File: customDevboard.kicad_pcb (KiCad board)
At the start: 2 copper layers, 39 x 39 mm, 79 parts, among them J1 USB_C_Receptacle_USB2.0_14P, J10 GPIO29_ADC3, J11 GND, J12 GPIO0, J13 GPIO1, J14 GPIO2, J15 GPIO3, J16 GPIO4, J17 GPIO5, J18 GPIO6, J19 GPIO7, J2 RUN, J20 GPIO8, J21 GPIO9, J22 Conn_01x01, J23 Conn_01x01, J24 Conn_01x01, J25 Conn_01x01, J26 Conn_01x01, J27 Conn_01x01, J28 Conn_01x01, J29 Conn_01x01, J3 3V3, J30 Conn_01x01, J31 Conn_01x01, J32 Conn_01x01, J33 Conn_01x01, J34 Conn_01x01, J35 Conn_01x01, J36 Conn_01x01, J37 Conn_01x01, J38 Conn_01x01, J39 Conn_01x01, J4 VBUS, J40 Conn_01x01, J41 Conn_01x01, J42 SWCLK, J43 GND, J44 SWD, J5 GND, J6 GND, J7 GPIO26_ADC0, J8 GPIO27_ADC1, J9 GPIO28_ADC2, SW1 BOOT, U1 RP2040, U2 W25Q128JVP, U3 TLV75733PDRV, Y1 12 MHz

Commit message: V1 testing release
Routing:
- net GND: vias 47 -> 48
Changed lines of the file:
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@@
+	)
+	(via
+		(at 66.5 72.5)
+		(size 0.6)
+		(drill 0.3)
+		(layers "F.Cu" "B.Cu")
+		(free yes)
+		(net 1)
 	)
 	(via
@@
 	)
 	(segment
+		(start 71.25 68.343656)
+		(end 71.25 67.75)
+		(width 0.2)
+		(layer "F.Cu")
+		(net 44)
+	)
+	(segment
+		(start 72.25 66.75)
+		(end 72.25 65.5)
+		(width 0.2)
+		(layer "F.Cu")
+		(net 44)
+	)
+	(segment
+		(start 72.5 70.5)
+		(end 71.25 69.25)
+		(width 0.2)
+		(layer "F.Cu")
+		(net 44)
+	)
+	(segment
+		(start 71.65 64.9)
+		(end 69.625 64.9)
+		(width 0.2)
+		(layer "F.Cu")
+		(net 44)
+	)
+	(segment
+		(start 71.25 68.493445)
+		(end 71.25 68.343656)
+		(width 0.2)
+		(layer "F.Cu")
+		(net 44)
+	)
+	(segment
 		(start 71.25 69.25)
+		(end 71.25 68.493445)
+		(width 0.2)
+		(layer "F.Cu")
+		(net 44)
+	)
+	(segment
+		(start 73.75 70.5)
 		(end 72.5 70.5)
 		(width 0.2)
@@
 	)
 	(segment
-		(start 72.25 66.75)
-		(end 71.25 67.75)
+		(start 72.25 65.5)
+		(end 71.65 64.9)
 		(width 0.2)
 		(layer "F.Cu")
@@
 	)
 	(segment
-		(start 72.5 70.5)
-		(end 73.75 70.5)
+		(start 71.25 67.75)
+		(end 72.25 66.75)
 		(width 0.2)
 		(layer "F.Cu")
@@
 	)
 	(segment
-		(start 71.65 64.9)
-		(end 72.25 65.5)
-		(width 0.2)
-		(layer "F.Cu")
-		(net 44)
-	)
-	(segment
-		(start 72.25 65.5)
-		(end 72.25 66.75)
-		(width 0.2)
-		(layer "F.Cu")
-		(net 44)
-	)
-	(segment
-		(start 69.625 64.9)
-		(end 71.65 64.9)
-		(width 0.2)
-		(layer "F.Cu")
-		(net 44)
-	)
-	(segment
-		(start 71.25 67.75)
-		(end 71.25 69.25)
-		(width 0.2)
-		(layer "F.Cu")
-		(net 44)
+		(start 70.75 68.523403)
+		(end 70.75 68.628255)
+		(width 0.2)
+		(layer "F.Cu")
+		(net 45)
+	)
+	(segment
+		(start 71.399 65.3)
+		(end 71.75 65.651)
+		(width 0.2)
+		(layer "F.Cu")
+		(net 45)
+	)
+	(segment
+		(start 69.625 65.3)
+		(end 71.399 65.3)
+		(width 0.2)
+		(layer "F.Cu")
+		(net 45)
+	)
+	(segment
+		(start 71.75 65.651)
+		(end 71.75 66.5)
+		(width 0.2)
+		(layer "F.Cu")
+		(net 45)
+	)
+	(segment
+		(start 70.75 68.628255)
+		(end 70.75 69.75)
+		(width 0.2)
+		(layer "F.Cu")
+		(net 45)
 	)
 	(segment
 		(start 71.75 66.5)
-		(end 71.75 65.651)
+		(end 70.75 67.5)
 		(width 0.2)
 		(layer "F.Cu")
@@
 	)
 	(segment
+		(start 70.75 67.5)
+		(end 70.75 68.523403)
+		(width 0.2)
+		(layer "F.Cu")
+		(net 45)
+	)
+	(segment
 		(start 72.5 71.5)
-		(end 70.75 69.75)
+		(end 73.74 71.5)
 		(width 0.2)
 		(layer "F.Cu")
@@
 	(segment
 		(start 70.75 69.75)
-		(end 70.75 67.5)
-		(width 0.2)
-		(layer "F.Cu")
-		(net 45)
-	)
-	(segment
-		(start 71.399 65.3)
-		(end 69.625 65.3)
-		(width 0.2)
-		(layer "F.Cu")
-		(net 45)
-	)
-	(segment
-		(start 70.75 67.5)
-		(end 71.75 66.5)
-		(width 0.2)
-		(layer "F.Cu")
-		(net 45)
-	)
-	(segment
-		(start 73.74 71.5)
 		(end 72.5 71.5)
-		(width 0.2)
-		(layer "F.Cu")
-		(net 45)
-	)
-	(segment
-		(start 71.75 65.651)
-		(end 71.399 65.3)
 		(width 0.2)
 		(layer "F.Cu")
@@
 		)
 	)
+	(generated
+		(type tuning_pattern)
+		(name "Tuning Pattern")
+		(layer "F.Cu")
+		(base_line
+			(pts
+				(xy 70.75 68.523403) (xy 70.75 68.628255)
+			)
+		)
+		(corner_radius_percent 80)
+		(end
+			(xy 70.75 68.628255)
+		)
+		(initial_side "left")
+		(last_diff_pair_gap 0.18)
+		(last_netname "Net-(U1-USB_DM)")
+		(last_status "tuned")
+		(last_track_width 0.2)
+		(last_tuning "10.4985 mm (tuned)")
+		(max_amplitude 1)
+		(min_amplitude 0.2)
+		(min_spacing 0.6)
+		(origin
+			(xy 70.75 68.523403)
+		)
+		(override_custom_rules no)
+		(rounded yes)
+		(single_sided no)
+		(target_length 1000000)
+		(target_length_max 1000000)
+		(target_length_min 0)
+		(target_skew 0)
+		(target_skew_max 0.1)
+		(target_skew_min -0.1)
+		(tuning_mode "single")
+		(members "117adbdf-2155-47f5-8e4f-017deaf49919")
+	)
+	(generated
+		(type tuning_pattern)
+		(name "Tuning Pattern")
+		(layer "F.Cu")
+		(base_line
+			(pts
+				(xy 71.25 68.493445) (xy 71.25 68.343656)
+			)
+		)
+		(corner_radius_percent 80)
+		(end
+			(xy 71.25 68.343656)
+		)
+		(initial_side "right")
+		(last_diff_pair_gap 0.18)
+		(last_netname "Net-(U1-USB_DP)")
+		(last_status "tuned")
+		(last_track_width 0.2)
+		(last_tuning "10.0555 mm (tuned)")
+		(max_amplitude 1)
+		(min_amplitude 0.2)
+		(min_spacing 0.6)
+		(origin
+			(xy 71.25 68.493445)
+		)
+		(override_custom_rules no)
+		(rounded yes)
+		(single_sided no)
+		(target_length 1000000)
+		(target_length_max 1000000)
+		(target_length_min 0)
+		(target_skew 0)
+		(target_skew_max 0.1)
+		(target_skew_min -0.1)
+		(tuning_mode "single")
+		(members "a65c19f3-3ae6-40a8-a287-4b1fe877de64")
+	)
 	(embedded_fonts no)

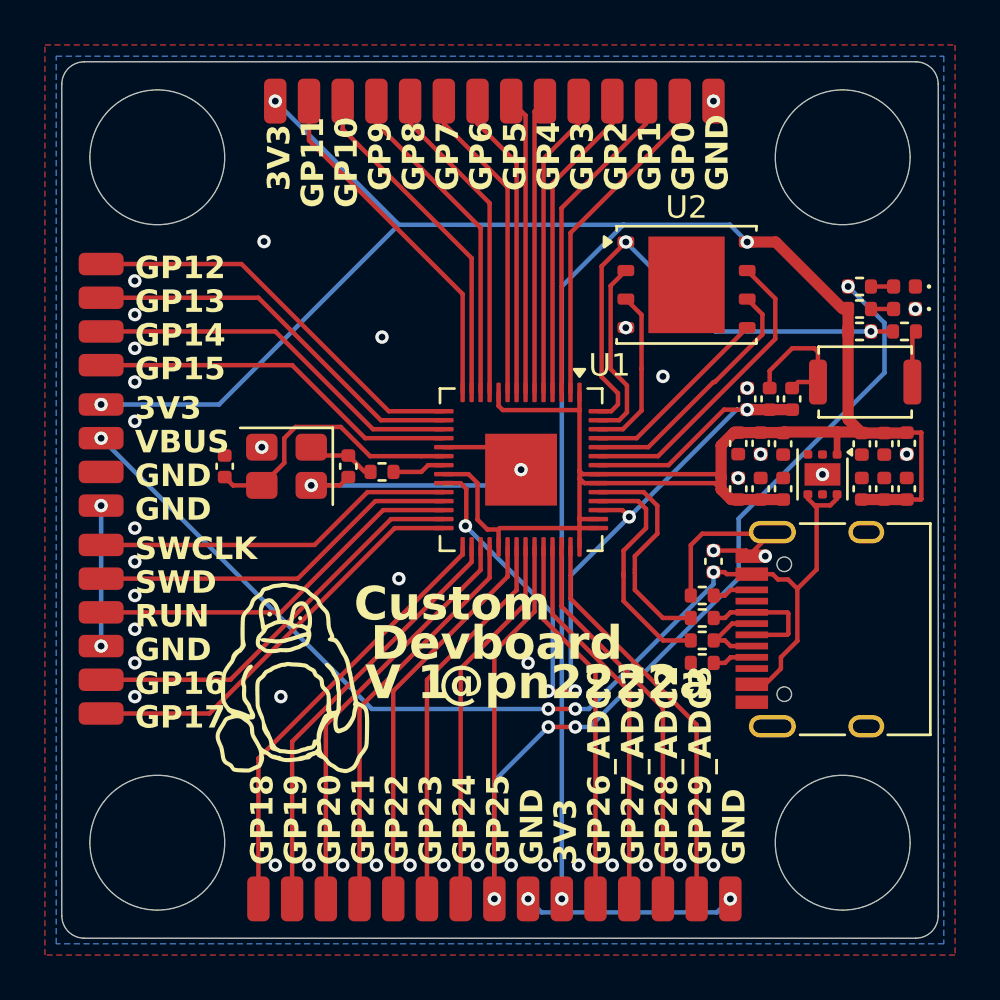
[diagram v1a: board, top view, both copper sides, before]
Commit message: fixed mounting hole size
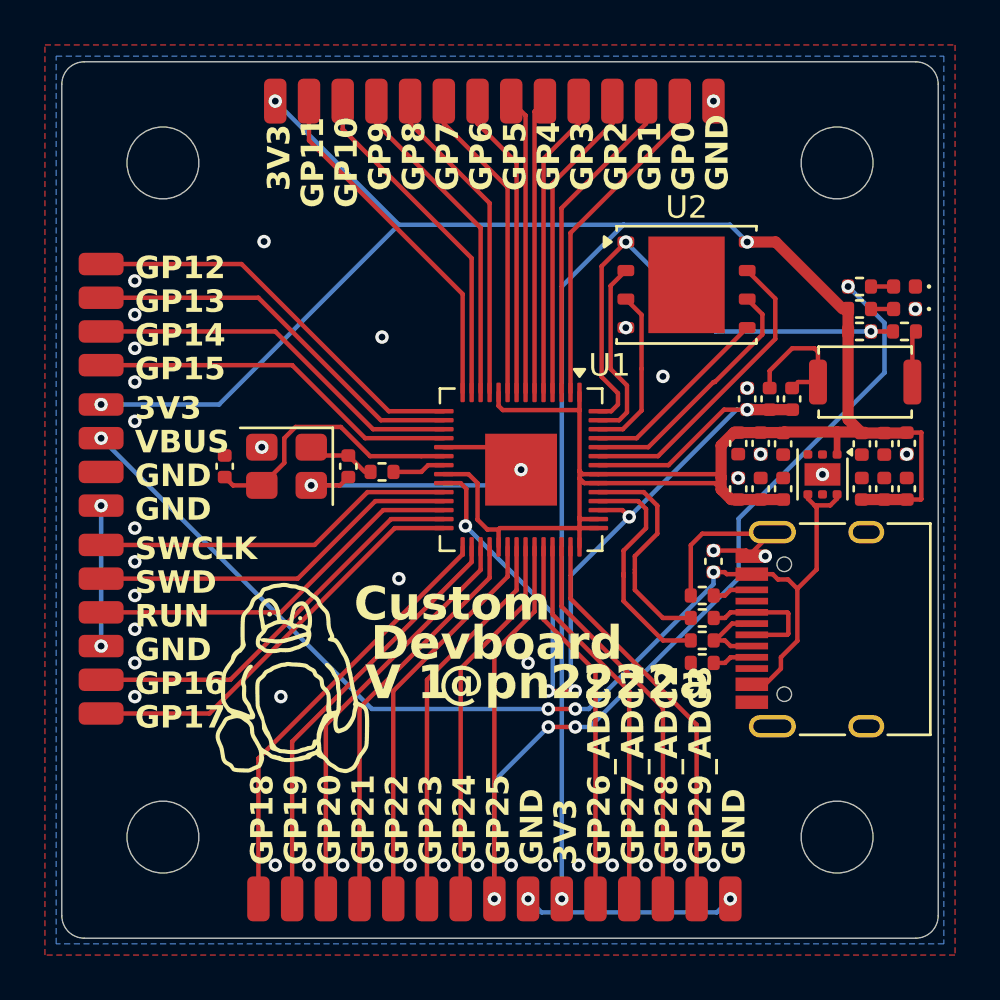
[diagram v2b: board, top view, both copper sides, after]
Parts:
- added REF**: MountingHole_3.2mm_M3, MountingHole:MountingHole_3.2mm_M3, F.Cu at (50.2, 80.2)
- added REF**: MountingHole_3.2mm_M3, MountingHole:MountingHole_3.2mm_M3, F.Cu at (80.2, 80.2)
- added REF**: MountingHole_3.2mm_M3, MountingHole:MountingHole_3.2mm_M3, F.Cu at (50.2, 50.2)
- added REF**: MountingHole_3.2mm_M3, MountingHole:MountingHole_3.2mm_M3, F.Cu at (80.2, 50.2)
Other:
- outline, holes or cut-outs redrawn
